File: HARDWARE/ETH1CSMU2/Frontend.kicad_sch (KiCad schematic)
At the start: 74 parts, among them Q601 MMBT3904, Q602 MMBT3904, Q603 MMBT3904, Q604 MMBT3904, U601 DG419DY, U602 DG419DY, U603 SN74LVC1T45DRLR, U604 SN74LVC1T45DRLR, U605 SN74LVC1T45DRLR, U606 LT1970ACFE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

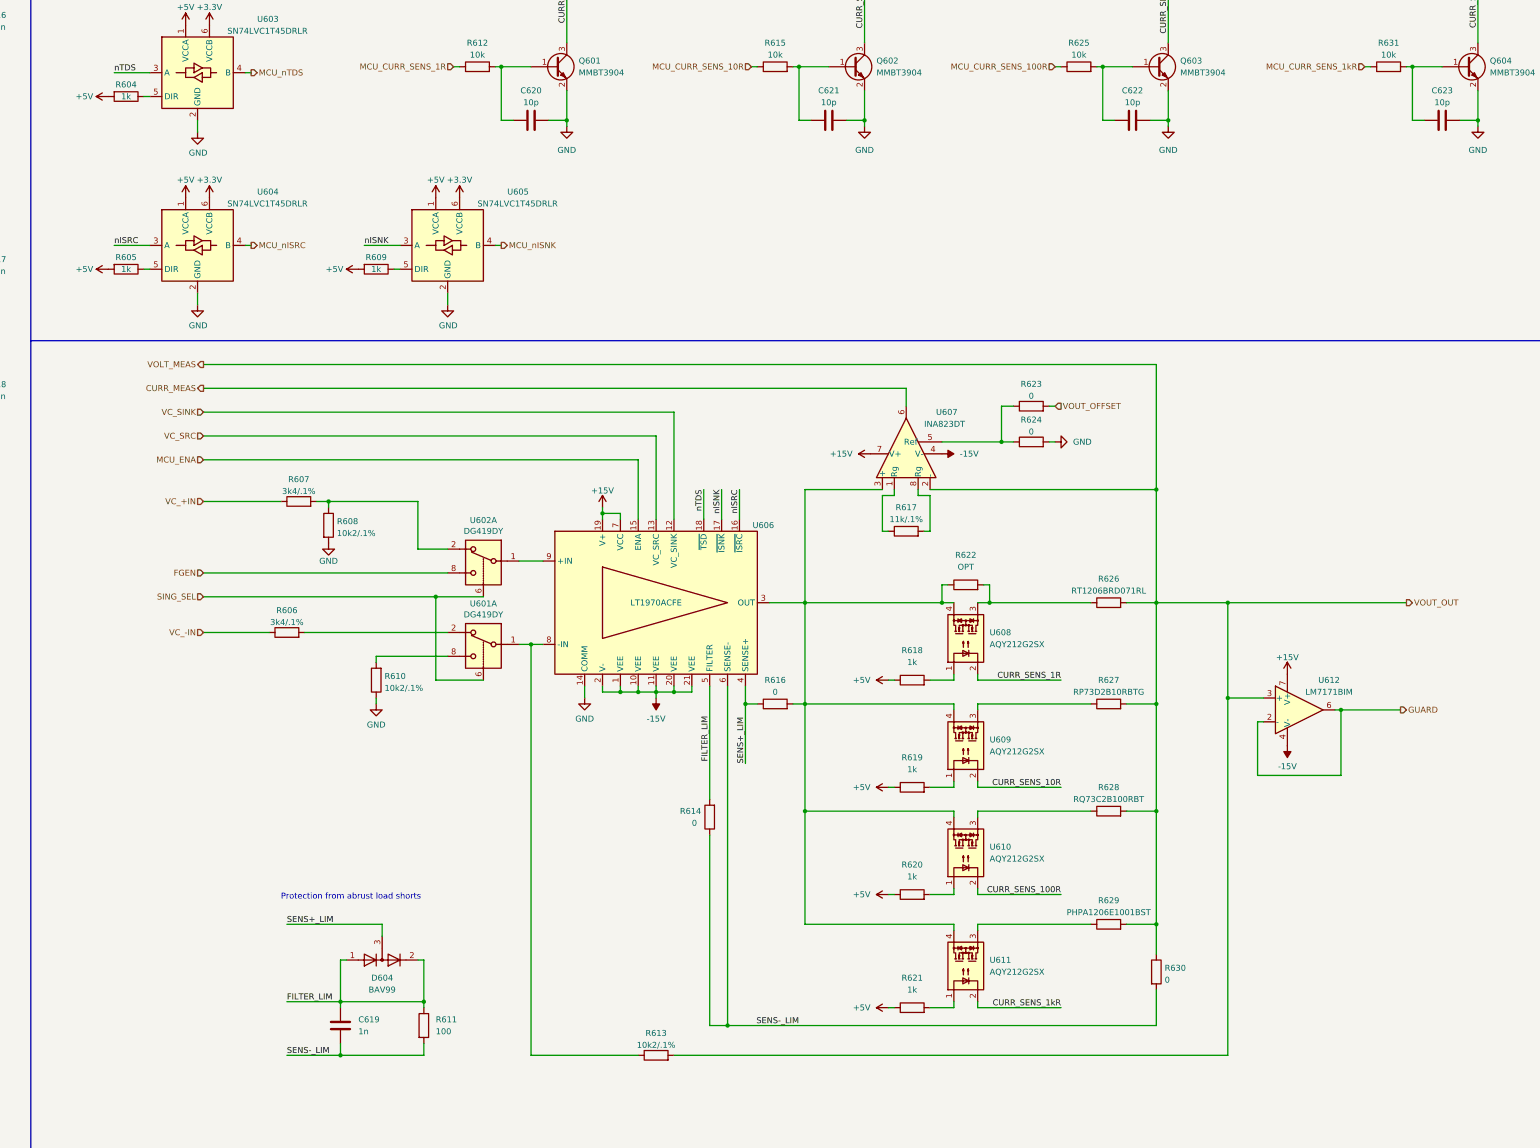
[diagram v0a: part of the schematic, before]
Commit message: Added two 10uF capacitors in Frontend page.
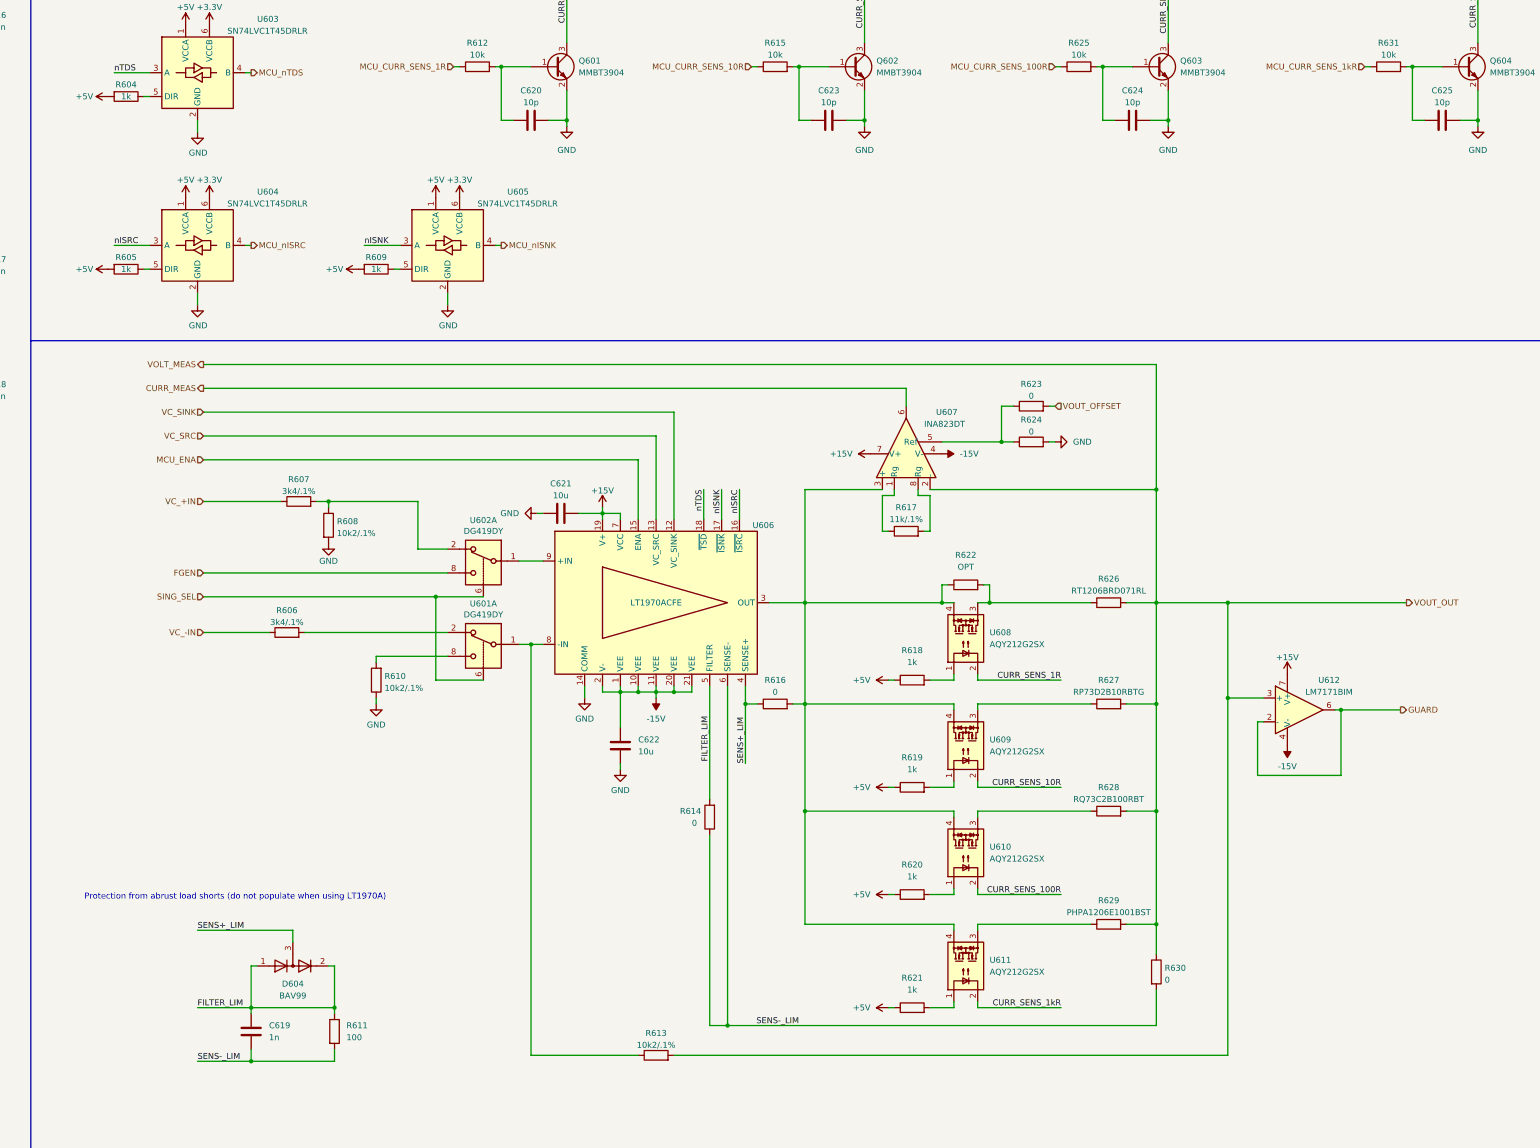
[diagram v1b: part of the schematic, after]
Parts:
- added C621, C622: 10u, Capacitor_SMD:C_1206_3216Metric_Pad1.33x1.80mm_HandSolder, symbol Device:C
- renumbered C621 to C623, C622 to C624, C623 to C625
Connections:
- net +15V: now also C621.2
- net -15V: now also C622.1
- net GND: now also C621.1, C622.2
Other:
- note added: "Protection from abrust load shorts (do not populate when using LT1970A)"
- note removed: "Protection from abrust load shorts"
- moved on the sheet: C619, D604, R611

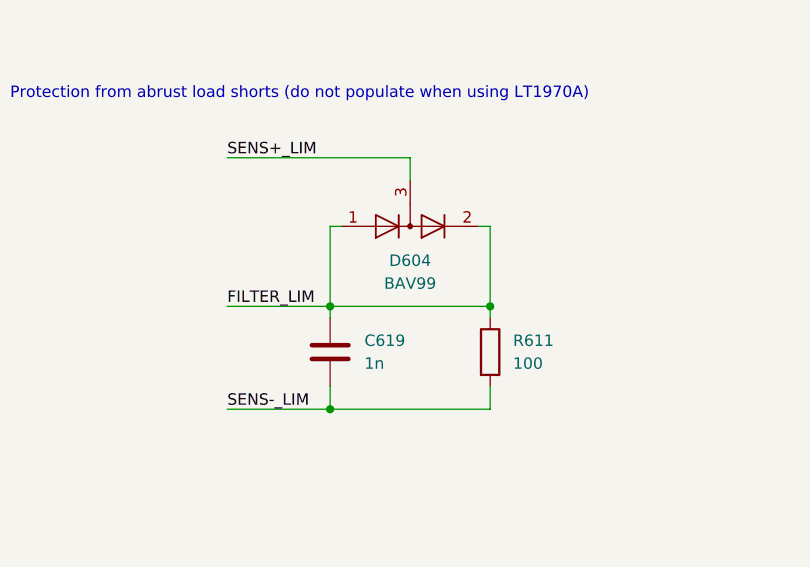
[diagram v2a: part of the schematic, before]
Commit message: Converter HW to KiCAD 7.0. Fixed 3D model paths.
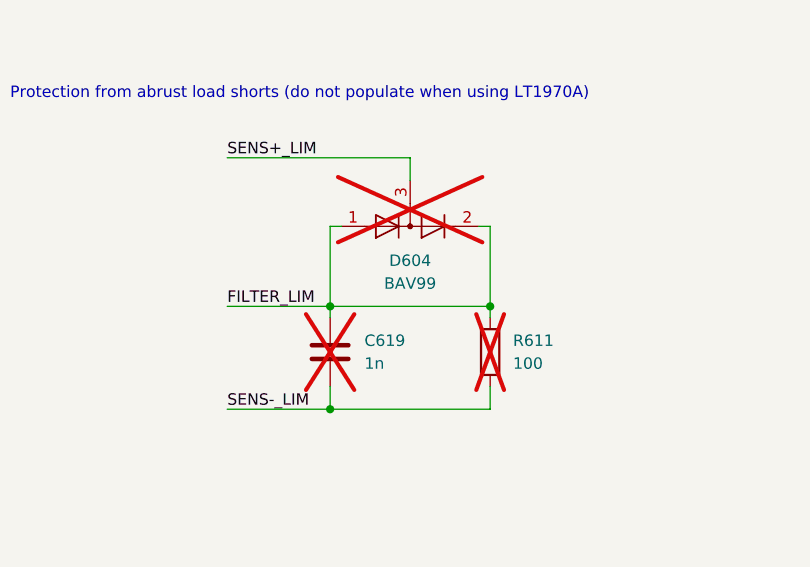
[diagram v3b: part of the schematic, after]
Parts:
- C619, D604, R611: now not fitted

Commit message: Software development
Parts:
- R622: now not fitted
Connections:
- net SING_SEL renamed SIGN_SEL
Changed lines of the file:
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@@
     (effects (font (size 1.27 1.27)) (justify right))
   )
-  (hierarchical_label "SING_SEL" (shape input) (at 118.11 152.4 180) (fields_autoplaced)
+  (hierarchical_label "SIGN_SEL" (shape input) (at 118.11 152.4 180) (fields_autoplaced)
     (effects (font (size 1.27 1.27)) (justify right))
   )
@@
   )
   (symbol (lib_id "Device:R") (at 280.67 149.86 90) (unit 1)
-    (in_bom yes) (on_board yes) (dnp no) (fields_autoplaced)
+    (in_bom yes) (on_board yes) (dnp yes) (fields_autoplaced)
     (property "Reference" "R622" (at 280.67 143.51 90)
       (effects (font (size 1.27 1.27)))

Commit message: Software development, added comments to schematic.
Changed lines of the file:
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@@
     (stroke (width 0) (type default))
+  )
+  (text_box "For selected FGEN the LT1970 gain is x2."
+    (at 90.17 184.15 0) (size 77.47 27.94)
+    (stroke (width 0) (type default))
+    (fill (type none))
+    (effects (font (size 1.27 1.27)) (justify left top))
   )
   (text "Protection from abrust load shorts (do not populate when using LT1970A)"

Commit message: Development
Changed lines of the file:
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@@
   )
   (polyline (pts (xy 81.28 97.79) (xy 406.4 97.79))
-    (stroke (width 0) (type default))
+    (stroke (width 0) (type dash))
   )
   (wire (pts (xy 55.88 24.13) (xy 43.18 24.13))
@@
   )
   (polyline (pts (xy 81.28 12.7) (xy 81.28 279.4))
-    (stroke (width 0) (type default))
+    (stroke (width 0) (type dash))
   )
   (wire (pts (xy 68.58 34.29) (xy 68.58 33.02))
@@
   )
   (text_box "For selected FGEN the LT1970 gain is x2."
-    (at 90.17 184.15 0) (size 77.47 27.94)
+    (at 99.06 167.64 0) (size 46.99 6.35)
     (stroke (width 0) (type default))
     (fill (type none))
@@
     (effects (font (size 1.27 1.27)) (justify left bottom))
   )
-  (text "MISC" (at 15.24 16.51 0)
-    (effects (font (size 1.27 1.27)) (justify left bottom))
-  )
-  (text "GPIO\n" (at 83.82 16.51 0)
-    (effects (font (size 1.27 1.27)) (justify left bottom))
+  (text "MISC" (at 15.24 17.78 0)
+    (effects (font (size 2.54 2.54) (thickness 0.508) bold) (justify left bottom))
+  )
+  (text "GPIO\n" (at 85.09 17.78 0)
+    (effects (font (size 2.54 2.54) (thickness 0.508) bold) (justify left bottom))
   )
   (label "nISNK" (at 152.4 77.47 0) (fields_autoplaced)

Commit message: Software development
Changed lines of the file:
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@@
     (stroke (width 0) (type default))
   )
-  (text_box "For selected FGEN the LT1970 gain is x2."
+  (text_box "For selected FGEN the LT1970 gain is x2.\nFor DC the LT1970 gain is x3."
     (at 99.06 167.64 0) (size 46.99 6.35)
     (stroke (width 0) (type default))
